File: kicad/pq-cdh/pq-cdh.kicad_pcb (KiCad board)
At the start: 4 copper layers, 43 x 43 mm, 35 parts, among them IC1 STM32L496RGT3, IC2 IS25LP128F-JBLA3, J1 Conn_01x04, J2 Conn_01x16, J3 Conn_01x04, J4 Conn_01x04, J5 Conn_01x16, J6 Conn_01x04, J7 Conn_02x06_Odd_Even, J8 Conn_01x04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

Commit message: gerber_update
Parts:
- C14, C7, C9: value 0603ZA220JAT2A -> 0603ZC104JAT2A
- C5, C6: value 0603ZA220JAT2A -> 0603ZC105JAT2A

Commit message: v0.2.0
Controller_adjustment
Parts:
- moved Y2 2.95 mm to (157.2, 113.9)
- moved C14 2.93 mm to (166.0, 92.5)
- moved R5 2.89 mm to (166.0, 90.9)
- moved IC2 2.82 mm to (166.0, 97.3)
- moved C5 1.97 mm to (155.8, 102.8)
- moved C6 1.97 mm to (155.8, 101.0)
- moved C7 1.97 mm to (158.8, 101.0)
- moved C8 1.97 mm to (158.8, 102.8)
- moved C9 1.97 mm to (155.7, 105.2)
- moved LED1 1.92 mm to (144.9, 122.1)
- moved LED2 1.91 mm to (147.9, 122.2)
- moved R4 1.91 mm to (151.8, 123.8)
- moved C2 1.91 mm to (142.6, 99.2)
- moved C3 1.91 mm to (149.1, 99.2)
- moved C4 1.91 mm to (151.8, 116.0)
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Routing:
- net /DCMI_D4: track 39.5 -> 35.6 mm
- net /DCMI_PIXCLK: track 28.7 -> 25.0 mm
- net /DCMI_D3: track 38.2 -> 34.7 mm
- net /DCMI_D2: track 40.3 -> 37.0 mm
- net /DCMI_D5: track 37.3 -> 34.0 mm
- net /DCMI_VSYNC: track 36.9 -> 33.7 mm
- net /DCMI_D7: track 30.9 -> 28.0 mm
- net /DCMI_HSYNC: track 32.7 -> 29.7 mm
- net /DCMI_D6: track 33.3 -> 30.5 mm
- net /DCMI_D0: track 43.2 -> 40.7 mm
- net /USART1_CTS: track 32.3 -> 30.2 mm
- net /VBAT: track 18.0 -> 15.9 mm
- net /DCMI_D1: track 40.9 -> 38.9 mm
- net GND: track 47.6 -> 45.6 mm
- net /USART1_RTS: track 40.5 -> 38.5 mm
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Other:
- board text added: "PQ CDH v0.2.0"
- board text removed: "PQ CDH v0.1.0"

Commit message: v0.1.1_updates
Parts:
- added TP: TP2, pq-cdh:TestPoint_Pad_D1.0mm, F.Cu at (159.4, 112.6)
- added TP: TP1, pq-cdh:TestPoint_Pad_D1.0mm, F.Cu at (159.4, 109.7)
- added TP: TP0, pq-cdh:TestPoint_Pad_D1.0mm, F.Cu at (159.4, 106.5)
- added TP: TP3, pq-cdh:TestPoint_Pad_D1.0mm, F.Cu at (159.4, 115.2)
- moved J1 38.1 mm to (174.1, 120.7)
- moved J8 38.1 mm to (135.9, 120.7)
- moved FB1 29.4 mm to (170.6, 116.9), turned to 180 degrees
- moved C1 29.2 mm to (170.5, 119.4), turned to 0 degrees
- moved R4 1.56 mm to (153.3, 123.6), turned to 0 degrees
- moved R3 1.55 mm to (153.3, 120.9), turned to 180 degrees
- moved Y2 0.33 mm to (156.9, 113.9)
- moved J6 0.09 mm to (155.1, 108.0)
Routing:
- net /SWDIO: track 18.7 -> 50.4 mm, vias 0 -> 1
- net /SWCLK: track 17.1 -> 42.7 mm, vias 0 -> 1
- net Net-(IC1-Pad60): track 11.3 -> 13.6 mm
- net GND: track 45.6 -> 43.8 mm
- net /BOOT0: track 3.94 -> 5.70 mm, vias 0 -> 1
- net VDD: track 4.37 -> 2.69 mm
- net Net-(C13-Pad1): track 11.5 -> 12.4 mm
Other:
- board text added: "PQ CDH v0.1.1"
- board text added: "TP0"
- board text added: "TP1"
- board text added: "TP2"
- board text added: "TP3"
- board text removed: "PQ CDH v0.2.0"

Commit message: v0.1.1_review_updates
remove vias for SWDIO and SWCLK and connecting directly to lower right connectors
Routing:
- net /SWDIO: track 50.4 -> 52.4 mm, vias 1 -> 0
- net /SWCLK: track 42.7 -> 42.9 mm, vias 1 -> 0
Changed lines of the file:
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@@
     (effects (font (size 0.5 0.5) (thickness 0.1)))
   )
-  (gr_text "FB1" (at 170.47 115.73) (layer "F.SilkS")
-    (effects (font (size 0.5 0.5) (thickness 0.1)))
-  )
-  (gr_text "C1" (at 170.6 120.62) (layer "F.SilkS")
+  (gr_text "FB1" (at 170.56 115.73) (layer "F.SilkS")
+    (effects (font (size 0.5 0.5) (thickness 0.1)))
+  )
+  (gr_text "C1" (at 170.51 120.6) (layer "F.SilkS")
     (effects (font (size 0.5 0.5) (thickness 0.1)))
   )
@@
   (via (at 163.53 112.65) (size 0.4572) (drill 0.254) (layers "F.Cu" "B.Cu") (net 3))
   (via (at 142.56 97.11) (size 0.4572) (drill 0.254) (layers "F.Cu" "B.Cu") (net 3))
-  (segment (start 142.56 114.5625) (end 142.56 122.45) (width 0.127) (layer "F.Cu") (net 5))
-  (segment (start 143.62648 125.24648) (end 170.48352 125.24648) (width 0.127) (layer "F.Cu") (net 5))
-  (segment (start 142.56 122.45) (end 142.56 124.18) (width 0.127) (layer "F.Cu") (net 5))
-  (segment (start 142.56 124.18) (end 143.62648 125.24648) (width 0.127) (layer "F.Cu") (net 5))
-  (segment (start 171.88 124.51) (end 171.14352 125.24648) (width 0.127) (layer "F.Cu") (net 5))
-  (segment (start 171.14352 125.24648) (end 170.48352 125.24648) (width 0.127) (layer "F.Cu") (net 5))
-  (segment (start 142.56 113.698) (end 142.56 114.5625) (width 0.127) (layer "F.Cu") (net 5))
-  (via (at 171.88 124.51) (size 0.4572) (drill 0.254) (layers "F.Cu" "B.Cu") (free) (net 5))
-  (segment (start 174.05 124.51) (end 171.88 124.51) (width 0.127) (layer "B.Cu") (net 5))
+  (segment (start 142.56 113.698) (end 142.56 124.18) (width 0.127) (layer "F.Cu") (net 5))
+  (segment (start 173.04352 125.51648) (end 169.08648 125.51648) (width 0.127) (layer "F.Cu") (net 5))
+  (segment (start 142.56 124.18) (end 143.89648 125.51648) (width 0.127) (layer "F.Cu") (net 5))
+  (segment (start 174.05 124.51) (end 173.04352 125.51648) (width 0.127) (layer "F.Cu") (net 5))
+  (segment (start 143.89648 125.51648) (end 169.08648 125.51648) (width 0.127) (layer "F.Cu") (net 5))
+  (segment (start 141.68 110.71) (end 140.572 110.71) (width 0.127) (layer "F.Cu") (net 6))
+  (segment (start 174.05 121.97) (end 175.19 123.11) (width 0.127) (layer "F.Cu") (net 6))
+  (segment (start 142.12 124.24) (end 142.12 111.15) (width 0.127) (layer "F.Cu") (net 6))
+  (segment (start 175.19 123.11) (end 175.19 125.14) (width 0.127) (layer "F.Cu") (net 6))
+  (segment (start 174.56 125.77) (end 143.65 125.77) (width 0.127) (layer "F.Cu") (net 6))
+  (segment (start 143.65 125.77) (end 142.12 124.24) (width 0.127) (layer "F.Cu") (net 6))
+  (segment (start 175.19 125.14) (end 174.56 125.77) (width 0.127) (layer "F.Cu") (net 6))
   (segment (start 142.12 111.15) (end 141.68 110.71) (width 0.127) (layer "F.Cu") (net 6))
-  (segment (start 142.12 124.24) (end 142.12 111.15) (width 0.127) (layer "F.Cu") (net 6))
-  (segment (start 143.38 125.5) (end 142.12 124.24) (width 0.127) (layer "F.Cu") (net 6))
-  (segment (start 141.68 110.71) (end 140.572 110.71) (width 0.127) (layer "F.Cu") (net 6))
-  (segment (start 172.41 124.75) (end 171.66 125.5) (width 0.127) (layer "F.Cu") (net 6))
-  (segment (start 171.66 125.5) (end 143.38 125.5) (width 0.127) (layer "F.Cu") (net 6))
-  (segment (start 172.41 121.97) (end 172.41 124.75) (width 0.127) (layer "F.Cu") (net 6))
-  (via (at 172.41 121.97) (size 0.4572) (drill 0.254) (layers "F.Cu" "B.Cu") (free) (net 6))
-  (segment (start 174.05 121.97) (end 172.41 121.97) (width 0.127) (layer "B.Cu") (net 6))
   (segment (start 174.05 116.89) (end 171.36 116.89) (width 0.127) (layer "F.Cu") (net 7))
   (segment (start 140.572 110.21) (end 143.91 110.21) (width 0.127) (layer "F.Cu") (net 11))

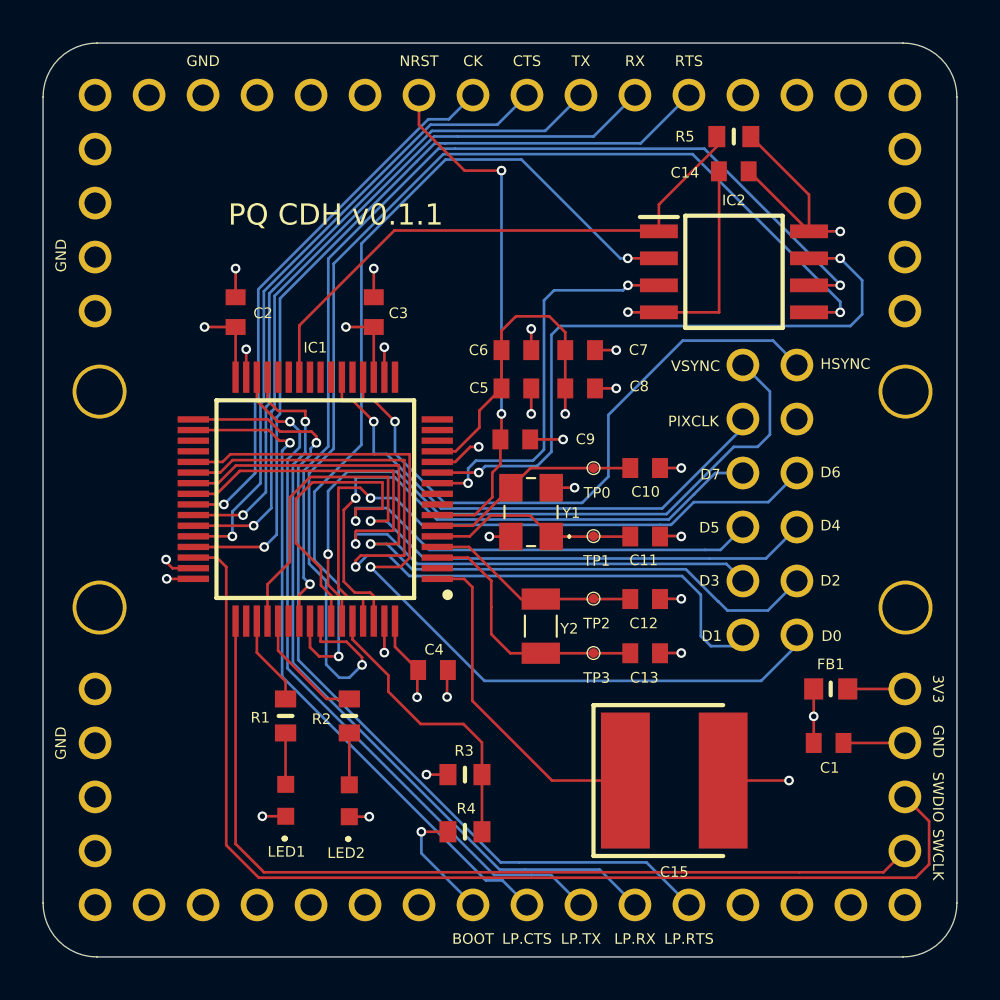
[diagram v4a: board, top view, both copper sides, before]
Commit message: pd_cdh_v0.2.0
- I2C3 SDA and SCL to pins 1 and 2 on the bottom header row
- ADC to pin 3 on the bottom header row
- unused GPIO to pins 4 and 5 on the bottom header row
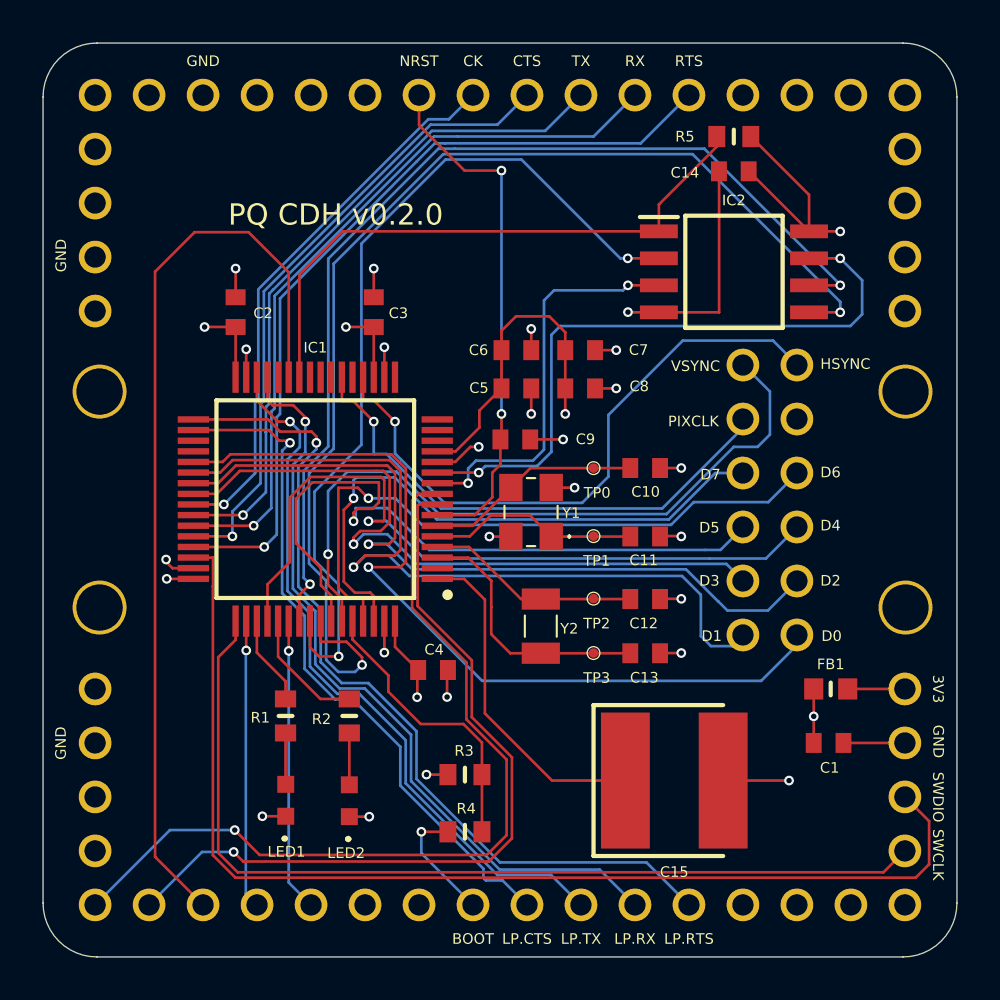
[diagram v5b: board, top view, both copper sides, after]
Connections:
- IC1 pad 27: unconnected-(IC1-Pad27) -> /AIN16
- IC1 pad 50: unconnected-(IC1-Pad50) -> /IO3
- IC1 pad 54: unconnected-(IC1-Pad54) -> /IO4
- IC1 pad 8: unconnected-(IC1-Pad8) -> /SCL3
- IC1 pad 9: unconnected-(IC1-Pad9) -> /SDA3
- J2 pad 1: unconnected-(J2-Pad1) -> /SDA3
- J2 pad 2: unconnected-(J2-Pad2) -> /SCL3
- J2 pad 3: unconnected-(J2-Pad3) -> /AIN16
- J2 pad 4: unconnected-(J2-Pad4) -> /IO3
- J2 pad 5: unconnected-(J2-Pad5) -> /IO4
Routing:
- net /AIN16: track 0.00 -> 43.5 mm
- net /SDA3: track 0.00 -> 40.6 mm, vias 0 -> 1
- net /SCL3: track 0.00 -> 37.2 mm, vias 0 -> 1
- net /IO4: track 0.00 -> 13.8 mm, vias 0 -> 1
- net /IO3: track 0.00 -> 13.6 mm, vias 0 -> 1
- net /SWCLK: track 42.9 -> 44.3 mm
- net /SPI1_NSS: track 26.8 -> 28.2 mm
- net /DCMI_D3: track 34.7 -> 33.7 mm
- net /DCMI_D1: track 38.9 -> 38.2 mm
- net /LPUART_RTS: track 40.1 -> 40.9 mm
- net /DCMI_D2: track 37.0 -> 36.3 mm
- net /SWDIO: track 52.4 -> 53.0 mm
- net /LPUART_RX: track 36.0 -> 36.5 mm
- net /LPUART_TX: track 33.5 -> 34.1 mm
- net /DCMI_D5: track 34.0 -> 33.5 mm
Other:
- board text added: "PQ CDH v0.2.0"
- board text removed: "PQ CDH v0.1.1"
